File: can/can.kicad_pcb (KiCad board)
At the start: 2 copper layers, 76.2 x 50.8 mm, 21 parts, among them J1 STM32WORLD_BOARD, J2 STM32WORLD_CONNECTOR_1, J3 STM32WORLD_CONNECTOR_2, U1 SN65HVD230DR, U2 SN65HVD230DR

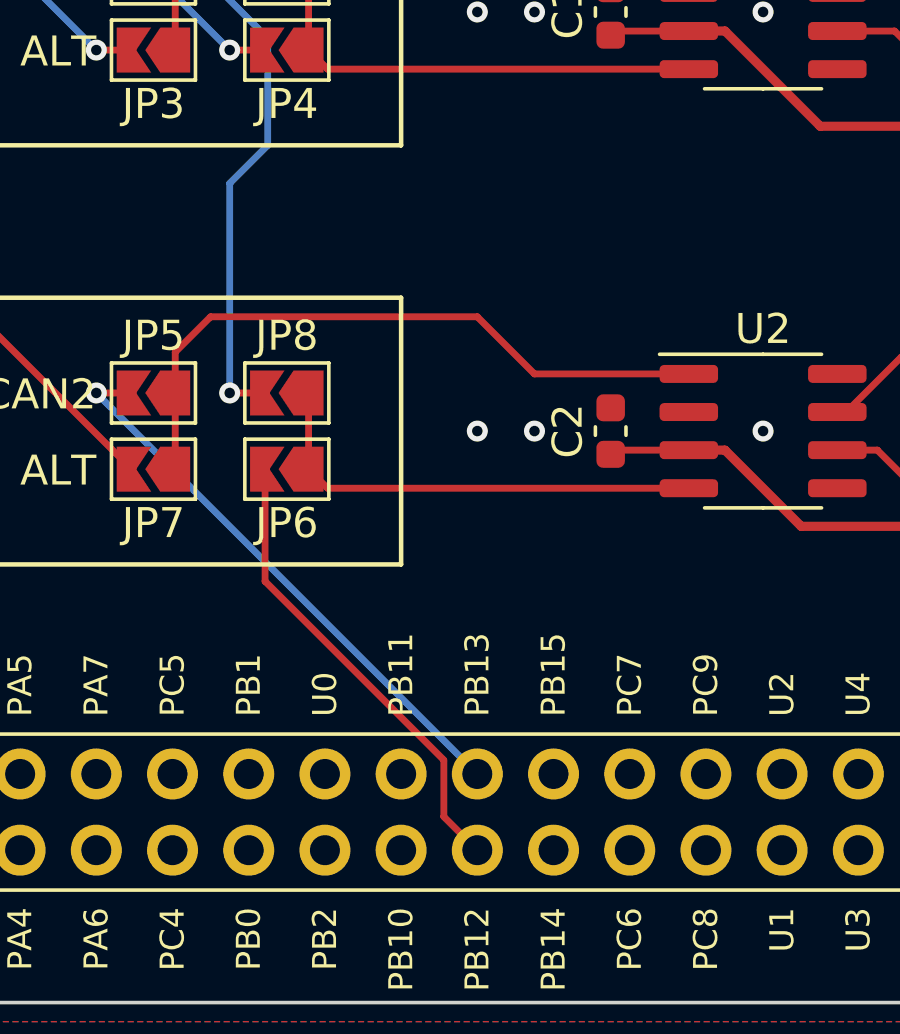
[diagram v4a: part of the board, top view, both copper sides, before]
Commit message: Fixed bug in cantrans
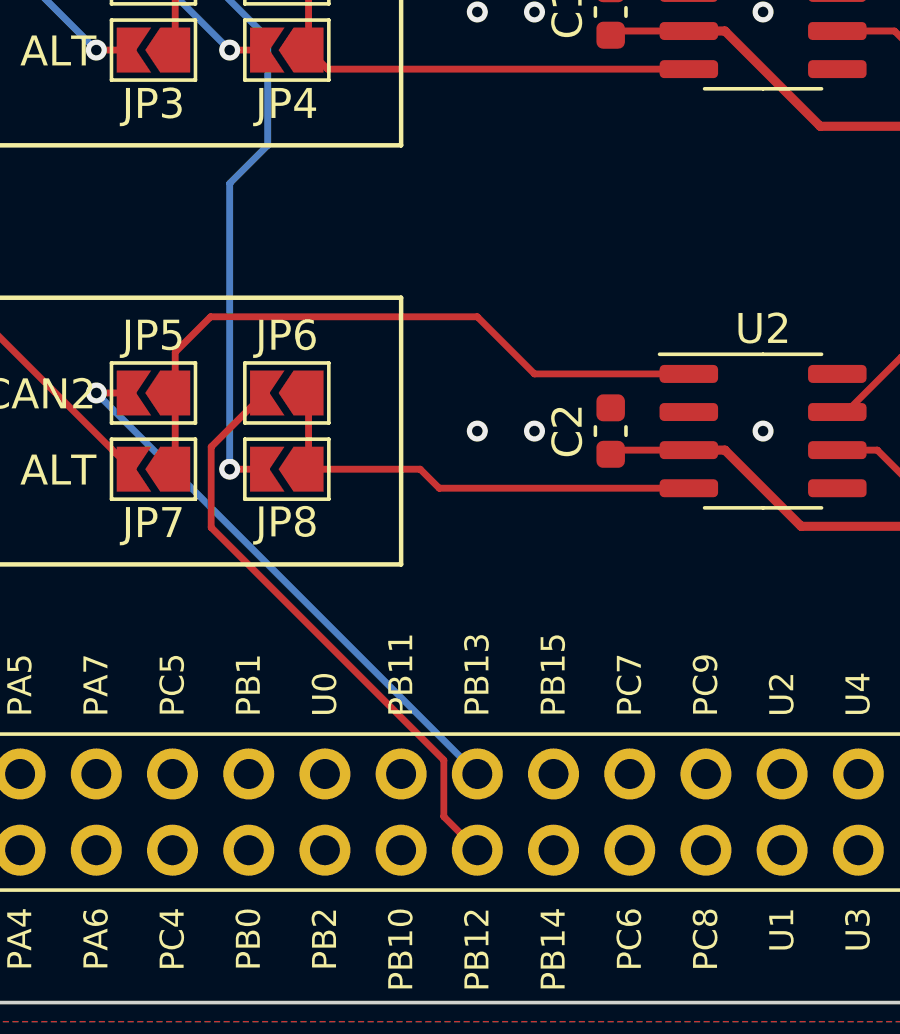
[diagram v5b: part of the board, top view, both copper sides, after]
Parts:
- moved JP6 2.54 mm to (149.9, 104.1)
- moved JP8 2.54 mm to (149.9, 106.7)
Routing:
- net CAN2_RX: track 15.6 -> 19.7 mm
- net CAN2_RX_A: track 26.9 -> 29.5 mm
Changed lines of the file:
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@@
   )
   (property "AUTHOR" "Lars Boegild Thomsen")
-  (property "AUTHOR_EMAIL" "lbthomsen@gmail.com")
-  (property "COMPANY" "stm32world")
+  (property "AUTHOR_EMAIL" "lbthomsen@stm32world.com")
+  (property "COMPANY" "STM32World")
   (property "REVISION" "b")
-  (property "TITLE" "can")
+  (property "TITLE" "CANTRANS")
   (property "URL" "https://stm32world.com/wiki/CANTRANS")
   (net 0 "")
@@
   )
   (footprint "Jumper:SolderJumper-2_P1.3mm_Open_TrianglePad1.0x1.5mm" (layer "F.Cu")
-    (at 149.86 104.14 180)
+    (at 149.86 106.68 180)
     (descr "SMD Solder Jumper, 1x1.5mm Triangular Pads, 0.3mm gap, open")
     (tags "solder jumper open")
@@
     (property "ki_keywords" "Jumper SPST")
     (attr exclude_from_pos_files)
-    (fp_text reference "JP8" (at 0 1.905) (layer "F.SilkS")
+    (fp_text reference "JP8" (at 0 -1.778) (layer "F.SilkS")
         (effects (font (size 1 1) (thickness 0.15)))
     )
@@
   )
   (footprint "Jumper:SolderJumper-2_P1.3mm_Open_TrianglePad1.0x1.5mm" (layer "F.Cu")
-    (at 149.86 106.68 180)
+    (at 149.86 104.14 180)
     (descr "SMD Solder Jumper, 1x1.5mm Triangular Pads, 0.3mm gap, open")
     (tags "solder jumper open")
@@
     (property "ki_keywords" "Jumper SPST")
     (attr exclude_from_pos_files)
-    (fp_text reference "JP6" (at 0 -1.8) (layer "F.SilkS")
+    (fp_text reference "JP6" (at 0 1.905) (layer "F.SilkS")
         (effects (font (size 1 1) (thickness 0.15)))
     )
@@
   (via (at 143.51 104.14) (size 0.7) (drill 0.35) (layers "F.Cu" "B.Cu") (net 25))
   (segment (start 143.51 104.14) (end 156.21 116.84) (width 0.2286) (layer "B.Cu") (net 25))
-  (segment (start 155.0933 118.2633) (end 156.21 119.38) (width 0.2286) (layer "F.Cu") (net 26))
-  (segment (start 149.135 110.419147) (end 155.0933 116.377447) (width 0.2286) (layer "F.Cu") (net 26))
-  (segment (start 149.135 106.68) (end 149.135 110.419147) (width 0.2286) (layer "F.Cu") (net 26))
-  (segment (start 155.0933 116.377447) (end 155.0933 118.2633) (width 0.2286) (layer "F.Cu") (net 26))
+  (segment (start 156.21 119.38) (end 155.0933 118.2633) (width 0.2286) (layer "F.Cu") (net 26))
+  (segment (start 147.3383 105.9367) (end 149.135 104.14) (width 0.2286) (layer "F.Cu") (net 26))
+  (segment (start 155.0933 118.2633) (end 155.0933 116.377447) (width 0.2286) (layer "F.Cu") (net 26))
+  (segment (start 155.0933 116.377447) (end 147.3383 108.622447) (width 0.2286) (layer "F.Cu") (net 26))
+  (segment (start 147.3383 108.622447) (end 147.3383 105.9367) (width 0.2286) (layer "F.Cu") (net 26))
   (segment (start 163.26 92.075) (end 164.234999 92.075) (width 0.2286) (layer "F.Cu") (net 37))
   (segment (start 167.005 108.585) (end 172.6048 108.585) (width 0.3048) (layer "F.Cu") (net 37))
@@
   (segment (start 150.925 83.185) (end 155.884253 83.185) (width 0.2286) (layer "F.Cu") (net 39))
   (segment (start 157.48 80.01) (end 158.75 78.74) (width 0.2286) (layer "F.Cu") (net 39))
-  (segment (start 149.135 104.14) (end 147.955 104.14) (width 0.2286) (layer "F.Cu") (net 42))
-  (via (at 147.955 104.14) (size 0.7) (drill 0.35) (layers "F.Cu" "B.Cu") (net 42))
+  (segment (start 149.135 106.68) (end 147.955 106.68) (width 0.2286) (layer "F.Cu") (net 42))
+  (via (at 147.955 106.68) (size 0.7) (drill 0.35) (layers "F.Cu" "B.Cu") (net 42))
+  (segment (start 147.955 97.155) (end 147.955 106.68) (width 0.2286) (layer "B.Cu") (net 42))
+  (segment (start 143.51 81.28) (end 146.05 83.82) (width 0.2286) (layer "B.Cu") (net 42))
   (segment (start 149.225 92.312146) (end 149.225 95.885) (width 0.2286) (layer "B.Cu") (net 42))
+  (segment (start 146.05 83.82) (end 146.05 89.137146) (width 0.2286) (layer "B.Cu") (net 42))
+  (segment (start 149.225 95.885) (end 147.955 97.155) (width 0.2286) (layer "B.Cu") (net 42))
   (segment (start 146.05 89.137146) (end 149.225 92.312146) (width 0.2286) (layer "B.Cu") (net 42))
-  (segment (start 143.51 81.28) (end 146.05 83.82) (width 0.2286) (layer "B.Cu") (net 42))
-  (segment (start 149.225 95.885) (end 147.955 97.155) (width 0.2286) (layer "B.Cu") (net 42))
-  (segment (start 146.05 83.82) (end 146.05 89.137146) (width 0.2286) (layer "B.Cu") (net 42))
-  (segment (start 147.955 97.155) (end 147.955 104.14) (width 0.2286) (layer "B.Cu") (net 42))
   (segment (start 139.8533 79.8567) (end 140.97 78.74) (width 0.2286) (layer "F.Cu") (net 50))
   (segment (start 144.69 106.68) (end 139.8533 101.8433) (width 0.2286) (layer "F.Cu") (net 50))
@@
   (segment (start 146.14 104.14) (end 146.14 102.78) (width 0.2286) (layer "F.Cu") (net 84))
   (segment (start 147.32 101.6) (end 156.21 101.6) (width 0.2286) (layer "F.Cu") (net 84))
-  (segment (start 151.22 107.315) (end 150.585 106.68) (width 0.2286) (layer "F.Cu") (net 85))
-  (segment (start 163.26 107.315) (end 151.22 107.315) (width 0.2286) (layer "F.Cu") (net 85))
-  (segment (start 150.585 106.68) (end 150.585 104.14) (width 0.2286) (layer "F.Cu") (net 85))
+  (segment (start 150.585 106.68) (end 154.305 106.68) (width 0.2286) (layer "F.Cu") (net 85))
+  (segment (start 150.585 104.14) (end 150.585 106.68) (width 0.2286) (layer "F.Cu") (net 85))
+  (segment (start 154.94 107.315) (end 163.26 107.315) (width 0.2286) (layer "F.Cu") (net 85))
+  (segment (start 154.305 106.68) (end 154.94 107.315) (width 0.2286) (layer "F.Cu") (net 85))
   (segment (start 171.995 90.17) (end 171.995 92.61) (width 0.2286) (layer "F.Cu") (net 86))
   (segment (start 171.995 92.61) (end 171.895 92.71) (width 0.2286) (layer "F.Cu") (net 86))
